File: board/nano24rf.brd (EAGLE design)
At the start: 17.8 x 42.9 mm, 19 parts

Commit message: pushed around
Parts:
- U$2: device Arduino-clone:NRF24-2X4 -> ATTAMI-V0.00:NRF24-2X4
- moved U$2 2.67 mm to (14.0, 33.0)
- moved C2 0.63 mm to (12.7, 19.1)
- turned FET1 to 180 degrees
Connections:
- net VCC renamed VOUT
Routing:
- net MOSI: track 13.1 -> 9.64 mm
- net CE: track 8.92 -> 6.91 mm
- net CSN: track 8.32 -> 6.93 mm
- net N$1: track 7.38 -> 8.51 mm
- net VOUT: track 4.07 -> 4.71 mm
- net 3V3: track 12.3 -> 12.0 mm, vias 1 -> 0

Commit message: more jump
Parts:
- moved SJ1 27.8 mm to (6.10, 29.3), turned to 180 degrees
- moved R3 1.78 mm to (9.02, 16.6), turned to 0 degrees
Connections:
- net 3V3: now also SJ1.2, SJ1.3
- net RAW: now also SJ1.1
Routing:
- net RAW: track 50.2 -> 56.7 mm
- net 3V3: track 12.0 -> 16.6 mm
- net VOUT: track 4.71 -> 7.51 mm
- net MOSI: track 9.64 -> 11.7 mm
- net GND: track 1.92 -> 3.70 mm, vias 0 -> 1
- net SCK: track 6.94 -> 8.23 mm
- added copper zone on layer 16, net GND
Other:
- board size 17.8 x 42.9 mm -> 17.8 x 40.3 mm
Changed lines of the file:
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@@
 <plain>
 <wire x1="0" y1="0" x2="17.76" y2="0" width="0" layer="20"/>
-<wire x1="17.76" y1="0" x2="17.76" y2="42.85" width="0" layer="20"/>
-<wire x1="17.76" y1="42.85" x2="0" y2="42.85" width="0" layer="20"/>
-<wire x1="0" y1="42.85" x2="0" y2="0" width="0" layer="20"/>
+<wire x1="17.76" y1="0" x2="17.76" y2="40.31" width="0" layer="20"/>
+<wire x1="17.76" y1="40.31" x2="0" y2="40.31" width="0" layer="20"/>
+<wire x1="0" y1="40.31" x2="0" y2="0" width="0" layer="20"/>
 <text x="0" y="1.27" size="1.7018" layer="21" align="bottom-right">D13
 3v3
@@
 <attribute name="VALUE" x="10.414" y="14.732" size="0.4064" layer="27" ratio="10" rot="R180"/>
 </element>
-<element name="SJ1" library="ATTAMI-V0.00" package="PAD-JUMPER-3-2OF3_NC_BY_TRACE_YES_SILK_LARGE" value="JUMPER-PAD-3-2OF3_NC_BY_TRACE_LARGE" x="29.21" y="13.97"/>
+<element name="SJ1" library="ATTAMI-V0.00" package="PAD-JUMPER-3-2OF3_NC_BY_TRACE_YES_SILK_LARGE" value="JUMPER-PAD-3-2OF3_NC_BY_TRACE_LARGE" x="6.096" y="29.337" smashed="yes" rot="R180">
+<attribute name="VALUE" x="6.1961" y="29.337" size="0.02" layer="27" rot="R180"/>
+</element>
 <element name="LM317" library="ATTAMI-V0.00" package="SOT89" value="" x="6.35" y="19.685" rot="R90"/>
 <element name="C1" library="ATTAMI-V0.00" package="0805" value="0.1uF" x="10.795" y="22.225" smashed="yes">
@@
 </element>
 <element name="C2" library="ATTAMI-V0.00" package="0805" value="1uF" x="12.7" y="19.05" smashed="yes" rot="R270">
-<attribute name="NAME" x="13.5255" y="20.32" size="0.4064" layer="25" rot="R270"/>
-</element>
-<element name="R3" library="ATTAMI-V0.00" package="0805" value="" x="10.795" y="16.51" smashed="yes" rot="R180">
-<attribute name="NAME" x="8.5725" y="17.272" size="0.8128" layer="25" rot="R270"/>
-<attribute name="VALUE" x="11.811" y="17.907" size="0.4064" layer="27" rot="R180"/>
+<attribute name="NAME" x="13.5255" y="20.32" size="0.8128" layer="25" rot="R270"/>
+</element>
+<element name="R3" library="ATTAMI-V0.00" package="0805" value="" x="9.017" y="16.637" smashed="yes">
+<attribute name="NAME" x="11.3665" y="16.002" size="0.8128" layer="25" rot="R90"/>
+<attribute name="VALUE" x="8.001" y="15.24" size="0.4064" layer="27"/>
 </element>
 <element name="R4" library="ATTAMI-V0.00" package="0805" value="" x="10.16" y="19.05" smashed="yes" rot="R270">
-<attribute name="NAME" x="10.8585" y="20.32" size="0.4064" layer="25" rot="R270"/>
+<attribute name="NAME" x="10.9855" y="20.32" size="0.8128" layer="25" rot="R270"/>
 <attribute name="VALUE" x="8.763" y="20.066" size="0.4064" layer="27" rot="R270"/>
 </element>
@@
 <contactref element="JP1" pad="14"/>
 <contactref element="JP2" pad="12"/>
-<contactref element="U$2" pad="GND"/>
-<wire x1="12.7" y1="18.15" x2="11.695" y2="16.51" width="0.4064" layer="1"/>
 <polygon width="0.254" layer="1">
 <vertex x="0" y="40.64"/>
@@
 <vertex x="17.78" y="1.27"/>
 <vertex x="17.78" y="40.64"/>
+</polygon>
+<contactref element="U$2" pad="GND"/>
+<wire x1="12.7" y1="35.56" x2="14.478" y2="32.639" width="0.254" layer="16"/>
+<via x="14.478" y="32.639" extent="1-16" drill="0.6" shape="square"/>
+<wire x1="14.478" y1="32.639" x2="14.605" y2="32.385" width="0.254" layer="1" curve="-9.527283"/>
+<polygon width="0.254" layer="16">
+<vertex x="0" y="40.005"/>
+<vertex x="0" y="0"/>
+<vertex x="17.526" y="0" curve="90"/>
+<vertex x="17.78" y="0.254"/>
+<vertex x="17.78" y="40.005"/>
 </polygon>
 </signal>
@@
 <wire x1="3.429" y1="3.937" x2="1.27" y2="2.54" width="0.6096" layer="16" curve="-31.734537"/>
 <wire x1="13.335" y1="2.54" x2="14.045" y2="6.35" width="0.6096" layer="1"/>
+<contactref element="SJ1" pad="1"/>
+<wire x1="7.62" y1="29.337" x2="7.62" y2="22.86" width="0.4064" layer="1"/>
 </signal>
 <signal name="N$2">
 <contactref element="Q1" pad="1"/>
 <contactref element="R1" pad="2"/>
-<wire x1="6.815" y1="11.841" x2="6.815" y2="13.408" width="0.254" layer="1"/>
 <wire x1="6.815" y1="13.408" x2="6.869" y2="13.843" width="0.254" layer="1"/>
+<wire x1="6.815" y1="13.408" x2="6.815" y2="11.841" width="0.254" layer="1"/>
 </signal>
 <signal name="D5">
@@
 <wire x1="9.895" y1="19.685" x2="10.16" y2="19.95" width="0.3048" layer="1"/>
 <wire x1="10.16" y1="19.95" x2="12.7" y2="19.95" width="0.254" layer="1"/>
-<wire x1="5.3" y1="19.685" x2="8.1" y2="19.685" width="0" layer="19" extent="1-1"/>
+<wire x1="5.3" y1="19.685" x2="8.1" y2="19.685" width="0.4064" layer="1"/>
 </signal>
 <signal name="N$7">
@@
 <wire x1="8.135" y1="18.15" x2="8.1" y2="18.185" width="0.3048" layer="1"/>
 <wire x1="10.16" y1="18.15" x2="9.895" y2="18.15" width="0.254" layer="1"/>
-<wire x1="9.895" y1="18.15" x2="9.895" y2="16.51" width="0.254" layer="1"/>
+<wire x1="9.895" y1="18.15" x2="9.917" y2="16.637" width="0.254" layer="1"/>
 </signal>
 <signal name="3V3">
 <contactref element="JP1" pad="2"/>
 <contactref element="U$2" pad="VCC"/>
-<wire x1="12.7" y1="33.02" x2="10.668" y2="34.036" width="0.4064" layer="1"/>
-<wire x1="10.668" y1="34.036" x2="9.779" y2="34.29" width="0.4064" layer="1" curve="21.239291"/>
-<wire x1="9.779" y1="34.29" x2="6.35" y2="34.29" width="0.4064" layer="1" curve="10.651379"/>
-<wire x1="6.35" y1="34.29" x2="3.683" y2="34.417" width="0.4064" layer="1" curve="-16.103986"/>
-<wire x1="3.683" y1="34.417" x2="1.27" y2="35.56" width="0.4064" layer="1" curve="-29.135786"/>
+<contactref element="SJ1" pad="2"/>
+<contactref element="SJ1" pad="3"/>
+<wire x1="12.7" y1="33.02" x2="11.303" y2="33.782" width="0.254" layer="1"/>
+<wire x1="11.303" y1="33.782" x2="10.541" y2="34.163" width="0.254" layer="1" curve="4.090817"/>
+<wire x1="10.541" y1="34.163" x2="9.271" y2="34.036" width="0.254" layer="1" curve="60.460491"/>
+<wire x1="9.271" y1="34.036" x2="9.017" y2="33.528" width="0.254" layer="1" curve="54.988408"/>
+<wire x1="9.017" y1="33.528" x2="8.382" y2="31.623" width="0.254" layer="1" curve="-38.728219"/>
+<wire x1="8.382" y1="31.623" x2="7.62" y2="30.988" width="0.254" layer="1" curve="-24.790814"/>
+<wire x1="7.62" y1="30.988" x2="6.096" y2="29.337" width="0.254" layer="1" curve="39.761004"/>
+<wire x1="1.27" y1="35.56" x2="4.572" y2="29.337" width="0.254" layer="1"/>
+<wire x1="4.572" y1="29.337" x2="4.826" y2="29.337" width="0" layer="19" extent="1-1"/>
 </signal>
 <signal name="MISO">
 <contactref element="U$2" pad="MISO"/>
 <contactref element="JP2" pad="1"/>
-<wire x1="5.08" y1="35.56" x2="6.477" y2="36.449" width="0.4064" layer="16"/>
-<wire x1="6.477" y1="36.449" x2="16.51" y2="38.1" width="0.4064" layer="16" curve="-46.253045"/>
+<wire x1="5.08" y1="35.56" x2="6.985" y2="36.957" width="0.254" layer="1"/>
+<wire x1="6.985" y1="36.957" x2="12.446" y2="38.227" width="0.254" layer="1" curve="-46.323894"/>
+<wire x1="12.446" y1="38.227" x2="16.51" y2="38.1" width="0.254" layer="1" curve="16.560243"/>
 </signal>
 <signal name="SCK">
 <contactref element="U$2" pad="SCK"/>
 <contactref element="JP1" pad="1"/>
-<wire x1="7.62" y1="35.56" x2="5.334" y2="37.084" width="0.4064" layer="1"/>
-<wire x1="5.334" y1="37.084" x2="1.27" y2="38.1" width="0.4064" layer="1" curve="39.307648"/>
+<wire x1="7.62" y1="35.56" x2="5.969" y2="34.544" width="0.254" layer="1"/>
+<wire x1="5.969" y1="34.544" x2="4.191" y2="34.671" width="0.254" layer="1" curve="-71.386128"/>
+<wire x1="4.191" y1="34.671" x2="1.27" y2="38.1" width="0.254" layer="1" curve="-19.590423"/>
 </signal>
 <signal name="CE">
 <contactref element="U$2" pad="CE"/>
 <contactref element="JP2" pad="3"/>
-<wire x1="10.16" y1="35.56" x2="11.811" y2="34.417" width="0.4064" layer="1"/>
-<wire x1="11.811" y1="34.417" x2="12.827" y2="34.036" width="0.4064" layer="1" curve="28.278211"/>
-<wire x1="12.827" y1="34.036" x2="16.51" y2="33.02" width="0.4064" layer="1" curve="-18.010577"/>
+<wire x1="10.16" y1="35.56" x2="11.684" y2="34.29" width="0.254" layer="1"/>
+<wire x1="11.684" y1="34.29" x2="12.192" y2="34.163" width="0.254" layer="1" curve="51.538861"/>
+<wire x1="12.192" y1="34.163" x2="16.51" y2="33.02" width="0.254" layer="1" curve="-53.119051"/>
 </signal>
 <signal name="CSN">
 <contactref element="U$2" pad="CSN"/>
 <contactref element="JP2" pad="4"/>
-<wire x1="10.16" y1="33.02" x2="13.081" y2="31.242" width="0.4064" layer="1"/>
-<wire x1="13.081" y1="31.242" x2="16.51" y2="30.48" width="0.4064" layer="1" curve="37.59977"/>
+<wire x1="10.16" y1="33.02" x2="12.954" y2="30.988" width="0.254" layer="16"/>
+<wire x1="12.954" y1="30.988" x2="16.51" y2="30.48" width="0.254" layer="16" curve="55.794551"/>
 </signal>
 <signal name="MOSI">
 <contactref element="U$2" pad="MOSI"/>
 <contactref element="JP2" pad="2"/>
-<wire x1="7.62" y1="33.02" x2="9.779" y2="34.163" width="0.4064" layer="16"/>
-<wire x1="9.779" y1="34.163" x2="10.795" y2="34.417" width="0.4064" layer="16" curve="-27.722047"/>
-<wire x1="10.795" y1="34.417" x2="15.24" y2="34.417" width="0.4064" layer="16" curve="-0.350277"/>
-<wire x1="15.24" y1="34.417" x2="16.51" y2="35.56" width="0.4064" layer="16" curve="84.321834"/>
+<wire x1="7.62" y1="33.02" x2="8.636" y2="34.544" width="0.254" layer="1"/>
+<wire x1="8.636" y1="34.544" x2="8.89" y2="35.433" width="0.254" layer="1" curve="35.489343"/>
+<wire x1="8.89" y1="35.433" x2="9.017" y2="36.449" width="0.254" layer="1" curve="-17.848341"/>
+<wire x1="9.017" y1="36.449" x2="10.033" y2="37.084" width="0.254" layer="1" curve="-83.891019"/>
+<wire x1="10.033" y1="37.084" x2="12.573" y2="37.084" width="0.254" layer="1" curve="19.880025"/>
+<wire x1="12.573" y1="37.084" x2="16.51" y2="35.56" width="0.254" layer="1" curve="-62.202581"/>
 </signal>
 <signal name="IRQ">

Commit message: add pdf, review ver
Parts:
- removed SJ2: JUMPER-PAD-2-NC_BY_TRACE, ATTAMI-V0.00:PAD-JUMPER-2-NC_BY_TRACE_YES_SILK
- removed SJ3: (no value), microbuilder:SOLDERJUMPER_REFLOW
- added SJ4: JUMPER-PAD-3-2OF3_NC_BY_TRACE_LARGE, ATTAMI-V0.00:PAD-JUMPER-3-2OF3_NC_BY_TRACE_YES_SILK_LARGE
- moved R1 5.11 mm to (6.48, 18.9)
- moved R2 5.09 mm to (12.8, 19.1)
- moved LM317 5.08 mm to (6.35, 24.8)
- moved Q1 5.08 mm to (5.71, 15.6)
- moved Q2 5.08 mm to (12.1, 15.6)
- moved C2 5.08 mm to (12.7, 24.1), turned to 90 degrees
- moved R4 5.08 mm to (10.2, 24.1)
- moved R3 4.97 mm to (9.40, 21.6), turned to 180 degrees
- moved C1 4.45 mm to (10.8, 26.7)
- moved SJ1 0.90 mm to (6.73, 28.7)
- turned D1 to 180 degrees
- turned D2 to 0 degrees
- turned FET2 to 0 degrees
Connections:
- new net 5V: JP1.12, JP2.13
- new net N$6: D1.1, D2.1, FET1.1, FET2.1, SJ4.2
- net GND: now also JP1.13, JP1.3
- net RAW: now also SJ4.3; no longer D1.1, D2.1, FET1.1, FET2.1
- net VOUT: now also SJ4.1
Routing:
- net RAW: track 56.7 -> 37.7 mm, vias 1 -> 3
- net 5V: track 0.00 -> 17.2 mm
- net VOUT: track 7.51 -> 22.8 mm, vias 0 -> 2
- net N$6: track 0.00 -> 14.6 mm
- net GND: track 3.70 -> 8.40 mm, vias 1 -> 2
- net N$4: track 7.59 -> 12.2 mm
- net N$1: track 8.51 -> 12.2 mm
- net D5: track 14.9 -> 11.6 mm
- net MOSI: track 11.7 -> 9.47 mm
- net SCK: track 8.23 -> 6.88 mm
- net D3: track 3.41 -> 4.72 mm
- net 3V3: track 16.6 -> 15.8 mm
- net N$7: track 3.85 -> 4.41 mm
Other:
- board text added: "D12 D11 D10 D9 D8 D7 D6 D5 D4 D3 D2 GND 5V RX TX"
- board text added: "D13 3v3 GND A0 A1 A2 A3 A4 A5 A6 A7 5V GND RAW"
- board text added: "GND"
- board text added: "SEshenkar"
- board text added: "nano24RF"
- board text added: "v1"
- board text removed: "D12 D11 D10 D9 D8 D7 D6 D5 D4 D3 D2 GND RST RX TX"
- board text removed: "D13 3v3 AREF A0 A1 A2 A3 A4 A5 A6 A7 5V RST GND RAW"

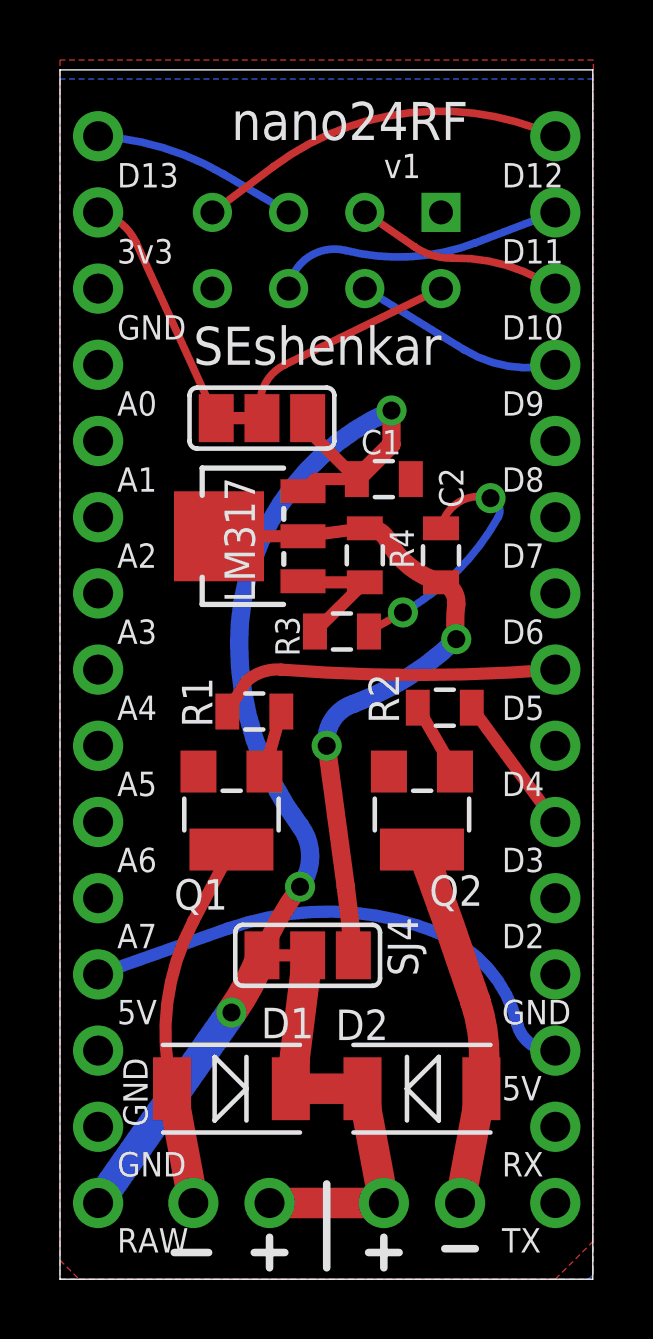
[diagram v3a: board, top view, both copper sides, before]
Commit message: rotate labels
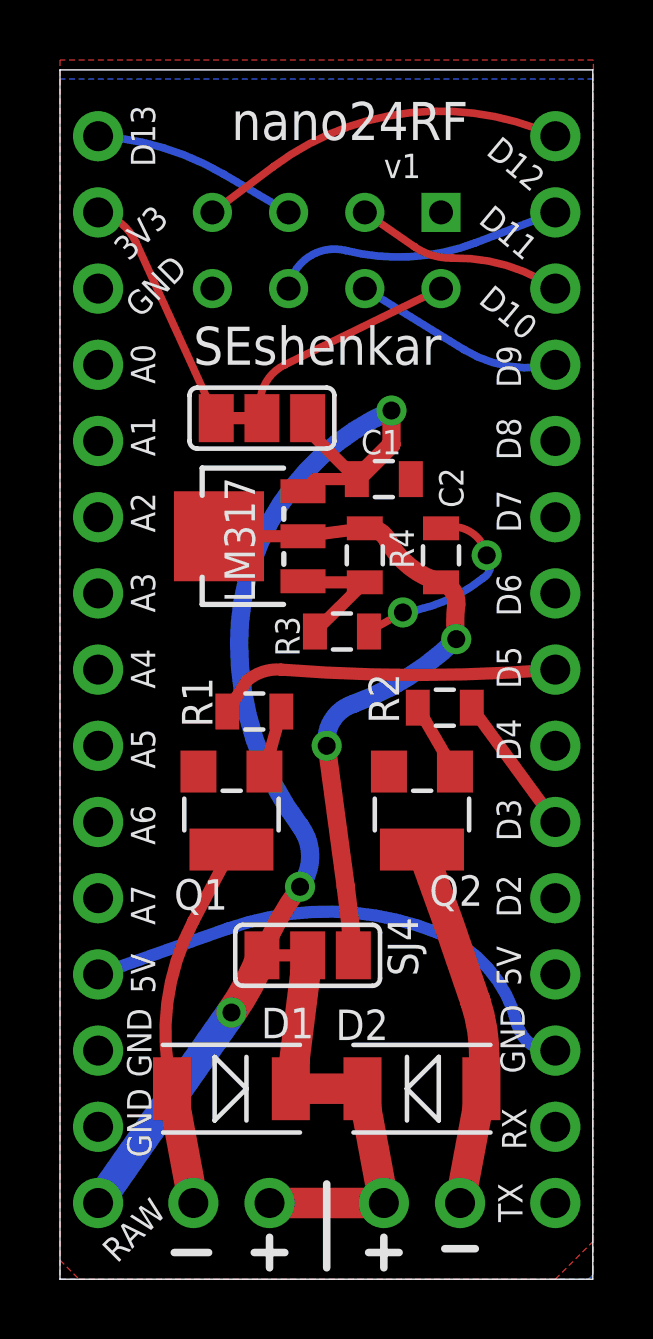
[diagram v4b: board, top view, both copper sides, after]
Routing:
- net GND: track 8.40 -> 6.74 mm
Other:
- board text added: "3V3"
- board text added: "5V"
- board text added: "A0"
- board text added: "A1"
- board text added: "A2"
- board text added: "A3"
- board text added: "A4"
- board text added: "A5"
- board text added: "A6"
- board text added: "A7"
- board text added: "D10"
- board text added: "D11"
- board text added: "D12"
- board text added: "D13"
- board text added: "D2"
- board text added: "D3"
- board text added: "D4"
- board text added: "D5"
- board text added: "D6"
- board text added: "D7"
- board text added: "D8"
- board text added: "D9"
- board text added: "RAW"
- board text added: "RX"
- board text added: "TX"
- board text removed: "D12 D11 D10 D9 D8 D7 D6 D5 D4 D3 D2 GND 5V RX TX"
- board text removed: "D13 3v3 GND A0 A1 A2 A3 A4 A5 A6 A7 5V GND RAW"
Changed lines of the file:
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@@
 <wire x1="17.76" y1="40.31" x2="0" y2="40.31" width="0" layer="20"/>
 <wire x1="0" y1="40.31" x2="0" y2="0" width="0" layer="20"/>
-<text x="1.905" y="0.889" size="0.8128" layer="21" font="vector" distance="212">D13
-3v3
-GND
-A0
-A1
-A2
-A3
-A4
-A5
-A6
-A7
-5V
-GND
-RAW</text>
-<text x="14.732" y="0.889" size="0.8128" layer="21" font="vector" distance="212">D12
-D11
-D10
-D9
-D8
-D7
-D6
-D5
-D4
-D3
-D2
-GND
-5V
-RX
-TX</text>
 <text x="4.445" y="30.48" size="1.27" layer="21" font="vector">SEshenkar</text>
 <text x="5.715" y="37.973" size="1.27" layer="21" font="vector">nano24RF</text>
 <text x="10.795" y="36.703" size="0.8128" layer="21" font="vector">v1</text>
-<text x="2.921" y="5.08" size="0.8128" layer="21" font="vector" rot="R90">GND</text>
 <wire x1="6.477" y1="0.889" x2="6.985" y2="0.889" width="0.254" layer="21"/>
 <wire x1="7.493" y1="0.889" x2="6.985" y2="0.889" width="0.254" layer="21"/>
@@
 <wire x1="4.953" y1="0.889" x2="3.81" y2="0.889" width="0.254" layer="21"/>
 <wire x1="8.89" y1="3.175" x2="8.89" y2="0.381" width="0.254" layer="21"/>
+<text x="14.605" y="1.905" size="0.8128" layer="21" font="vector" distance="212" rot="R270" align="bottom-right">TX</text>
+<text x="14.732" y="4.318" size="0.8128" layer="21" font="vector" distance="212" rot="R270" align="bottom-right">RX</text>
+<text x="15.367" y="9.779" size="0.8128" layer="21" font="vector" rot="R90">5V</text>
+<text x="15.494" y="6.858" size="0.8128" layer="21" font="vector" rot="R90">GND</text>
+<text x="15.367" y="12.065" size="0.8128" layer="21" font="vector" rot="R90">D2</text>
+<text x="15.367" y="14.605" size="0.8128" layer="21" font="vector" rot="R90">D3</text>
+<text x="15.367" y="17.272" size="0.8128" layer="21" font="vector" rot="R90">D4</text>
+<text x="15.367" y="19.685" size="0.8128" layer="21" font="vector" rot="R90">D5</text>
+<text x="15.367" y="22.098" size="0.8128" layer="21" font="vector" rot="R90">D6</text>
+<text x="15.367" y="24.892" size="0.8128" layer="21" font="vector" rot="R90">D7</text>
+<text x="15.367" y="27.305" size="0.8128" layer="21" font="vector" rot="R90">D8</text>
+<text x="15.367" y="29.718" size="0.8128" layer="21" font="vector" rot="R90">D9</text>
+<text x="16.002" y="31.877" size="0.8128" layer="21" font="vector" rot="R140">D10</text>
+<text x="16.002" y="34.544" size="0.8128" layer="21" font="vector" rot="R140">D11</text>
+<text x="16.256" y="36.83" size="0.8128" layer="21" font="vector" rot="R140">D12</text>
+<text x="1.905" y="0.508" size="0.8128" layer="21" font="vector" rot="R45">RAW</text>
+<text x="3.048" y="6.731" size="0.8128" layer="21" font="vector" rot="R90">GND</text>
+<text x="3.175" y="9.525" size="0.8128" layer="21" font="vector" rot="R90">5V</text>
+<text x="3.175" y="11.811" size="0.8128" layer="21" font="vector" rot="R90">A7</text>
+<text x="3.175" y="14.478" size="0.8128" layer="21" font="vector" rot="R90">A6</text>
+<text x="3.175" y="17.018" size="0.8128" layer="21" font="vector" rot="R90">A5</text>
+<text x="3.175" y="19.685" size="0.8128" layer="21" font="vector" rot="R90">A4</text>
+<text x="3.175" y="22.225" size="0.8128" layer="21" font="vector" rot="R90">A3</text>
+<text x="3.175" y="24.892" size="0.8128" layer="21" font="vector" rot="R90">A2</text>
+<text x="3.175" y="27.432" size="0.8128" layer="21" font="vector" rot="R90">A1</text>
+<text x="3.175" y="29.845" size="0.8128" layer="21" font="vector" rot="R90">A0</text>
+<text x="2.667" y="32.004" size="0.8128" layer="21" font="vector" rot="R45">GND</text>
+<text x="2.286" y="33.909" size="0.8128" layer="21" font="vector" rot="R45">3V3</text>
+<text x="3.175" y="37.084" size="0.8128" layer="21" font="vector" rot="R90">D13</text>
+<text x="3.048" y="4.064" size="0.8128" layer="21" font="vector" rot="R90">GND</text>
 </plain>
 <attributes>
@@
 <wire x1="10.298" y1="21.59" x2="11.43" y2="22.225" width="0.254" layer="1"/>
 <via x="11.43" y="22.225" extent="1-16" drill="0.6" shape="square"/>
-<wire x1="11.43" y1="22.225" x2="14.605" y2="25.4" width="0.254" layer="16" curve="31.419148"/>
-<wire x1="14.605" y1="25.4" x2="14.351" y2="26.035" width="0.254" layer="16" curve="102.183515"/>
-<via x="14.351" y="26.035" extent="1-16" drill="0.6" shape="square"/>
-<wire x1="14.351" y1="26.035" x2="12.7" y2="25.03" width="0.254" layer="1" curve="96.873172"/>
+<wire x1="11.43" y1="22.225" x2="14.097" y2="23.368" width="0.254" layer="16" curve="31.419148"/>
+<wire x1="14.097" y1="23.368" x2="14.224" y2="24.13" width="0.254" layer="16" curve="102.183515"/>
+<via x="14.224" y="24.13" extent="1-16" drill="0.6" shape="square"/>
+<wire x1="14.224" y1="24.13" x2="12.7" y2="25.03" width="0.254" layer="1" curve="96.873172"/>
 <contactref element="JP1" pad="3"/>
 </signal>
@@
 </board>
 </drawing>
-<compatibility>
-<note version="6.3" minversion="6.2.2" severity="warning">
-Since Version 6.2.2 text objects can contain more than one line,
-which will not be processed correctly with this version.
-</note>
-</compatibility>
 </eagle>
